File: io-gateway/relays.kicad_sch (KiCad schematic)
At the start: 24 parts, among them K1 2071556-2, K2 2071556-2, K3 2071556-2, K4 2071556-2, K5 2071556-2, K6 2071556-2, Q1 NTR4003NT1G, Q2 NTR4003NT1G, Q3 NTR4003NT1G, Q4 NTR4003NT1G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

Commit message: layout for first dimmer
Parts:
- K1, K2, K3, K4, K5, K6: footprint 20715562 -> Relay:20715562
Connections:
- net VAC_IN_1: no longer K2.4 (NO)
- net VAC_IN_2: now also K2.4 (NO); no longer K3.4 (NO), K4.4 (NO)
- net VAC_IN_3: now also K3.4 (NO); no longer K5.4 (NO), K6.4 (NO)
- net VAC_OUT_1.1 renamed VAC_OUT_1
- net VAC_OUT_1.2 renamed VAC_OUT_2
- net VAC_OUT_2.1 renamed VAC_OUT_3
- net VAC_OUT_2.2 renamed VAC_OUT_4
- net VAC_OUT_3.1 renamed VAC_OUT_5
- net VAC_OUT_3.2 renamed VAC_OUT_6
- new net VAC_IN_4: K4.4 (NO)
- new net VAC_IN_5: K5.4 (NO)
- new net VAC_IN_6: K6.4 (NO)
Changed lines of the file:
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@@
 	(wire
 		(pts
+			(xy 129.54 38.1) (xy 129.54 45.72)
+		)
+		(stroke
+			(width 0)
+			(type default)
+		)
+	)
+	(wire
+		(pts
 			(xy 190.5 40.64) (xy 190.5 46.99)
 		)
@@
 	(wire
 		(pts
-			(xy 35.56 58.42) (xy 35.56 71.12)
+			(xy 200.66 72.39) (xy 200.66 67.31)
 		)
 		(stroke
@@
 	(wire
 		(pts
-			(xy 119.38 152.4) (xy 119.38 157.48)
+			(xy 35.56 58.42) (xy 35.56 71.12)
 		)
 		(stroke
@@
 	(wire
 		(pts
-			(xy 204.47 38.1) (xy 200.66 38.1)
+			(xy 119.38 152.4) (xy 119.38 157.48)
 		)
 		(stroke
@@
 	(wire
 		(pts
+			(xy 129.54 72.39) (xy 137.16 72.39)
+		)
+		(stroke
+			(width 0)
+			(type default)
+		)
+	)
+	(wire
+		(pts
 			(xy 102.87 58.42) (xy 102.87 71.12)
 		)
@@
 	(wire
 		(pts
-			(xy 200.66 67.31) (xy 200.66 80.01)
-		)
-		(stroke
-			(width 0)
-			(type default)
-		)
-	)
-	(wire
-		(pts
 			(xy 190.5 67.31) (xy 190.5 72.39)
 		)
@@
 	(wire
 		(pts
-			(xy 129.54 72.39) (xy 138.43 72.39)
+			(xy 213.36 102.87) (xy 196.85 102.87)
 		)
 		(stroke
@@
 	(wire
 		(pts
-			(xy 213.36 102.87) (xy 196.85 102.87)
+			(xy 190.5 91.44) (xy 190.5 95.25)
 		)
 		(stroke
@@
 	(wire
 		(pts
-			(xy 190.5 91.44) (xy 190.5 95.25)
+			(xy 63.5 151.13) (xy 62.23 151.13)
 		)
 		(stroke
@@
 	(wire
 		(pts
-			(xy 63.5 151.13) (xy 62.23 151.13)
+			(xy 173.99 83.82) (xy 180.34 83.82)
 		)
 		(stroke
@@
 	(wire
 		(pts
-			(xy 173.99 83.82) (xy 180.34 83.82)
+			(xy 62.23 44.45) (xy 62.23 38.1)
 		)
 		(stroke
@@
 	(wire
 		(pts
-			(xy 62.23 44.45) (xy 62.23 38.1)
+			(xy 213.36 129.54) (xy 213.36 134.62)
 		)
 		(stroke
@@
 	(wire
 		(pts
-			(xy 213.36 129.54) (xy 213.36 134.62)
+			(xy 196.85 102.87) (xy 196.85 114.3)
 		)
 		(stroke
@@
 	(wire
 		(pts
-			(xy 196.85 102.87) (xy 196.85 114.3)
+			(xy 200.66 38.1) (xy 204.47 38.1)
 		)
 		(stroke
@@
 	(wire
 		(pts
-			(xy 190.5 40.64) (xy 173.99 40.64)
+			(xy 204.47 72.39) (xy 200.66 72.39)
 		)
 		(stroke
@@
 	(wire
 		(pts
-			(xy 129.54 40.64) (xy 129.54 45.72)
+			(xy 190.5 40.64) (xy 173.99 40.64)
 		)
 		(stroke
@@
 	(wire
 		(pts
+			(xy 134.62 38.1) (xy 129.54 38.1)
+		)
+		(stroke
+			(width 0)
+			(type default)
+		)
+	)
+	(wire
+		(pts
 			(xy 35.56 163.83) (xy 41.91 163.83)
 		)
@@
 		)
 	)
-	(global_label "VAC_IN_3"
+	(global_label "VAC_IN_5"
 		(shape input)
 		(at 132.08 156.21 0)
@@
 		)
 	)
-	(global_label "VAC_OUT_1.2"
+	(global_label "VAC_IN_3"
 		(shape input)
-		(at 129.54 40.64 0)
+		(at 204.47 72.39 0)
 		(fields_autoplaced yes)
 		(effects
@@
 		)
 		(property "Intersheetrefs" "${INTERSHEET_REFS}"
-			(at 144.56 40.64 0)
+			(at 215.9824 72.39 0)
 			(effects
 				(font
@@
 		)
 	)
-	(global_label "VAC_IN_1"
+	(global_label "VAC_IN_4"
 		(shape input)
-		(at 138.43 72.39 0)
+		(at 63.5 151.13 0)
 		(fields_autoplaced yes)
 		(effects
@@
 		)
 		(property "Intersheetrefs" "${INTERSHEET_REFS}"
-			(at 149.9424 72.39 0)
+			(at 75.0124 151.13 0)
 			(effects
 				(font
@@
 	(global_label "VAC_IN_2"
 		(shape input)
-		(at 200.66 80.01 0)
+		(at 137.16 72.39 0)
 		(fields_autoplaced yes)
 		(effects
@@
 		)
 		(property "Intersheetrefs" "${INTERSHEET_REFS}"
-			(at 212.1724 80.01 0)
+			(at 148.6724 72.39 0)
 			(effects
 				(font
@@
 		)
 	)
-	(global_label "VAC_IN_2"
+	(global_label "VAC_IN_6"
 		(shape input)
-		(at 63.5 151.13 0)
+		(at 226.06 134.62 0)
 		(fields_autoplaced yes)
 		(effects
@@
 		)
 		(property "Intersheetrefs" "${INTERSHEET_REFS}"
-			(at 75.0124 151.13 0)
+			(at 237.5724 134.62 0)
 			(effects
 				(font
@@
 		)
 	)
-	(global_label "VAC_IN_3"
+	(global_label "VAC_OUT_5"
 		(shape input)
-		(at 226.06 134.62 0)
+		(at 132.08 125.73 0)
 		(fields_autoplaced yes)
 		(effects
@@
 		)
 		(property "Intersheetrefs" "${INTERSHEET_REFS}"
-			(at 237.5724 134.62 0)
+			(at 145.2857 125.73 0)
 			(effects
 				(font
@@
 		)
 	)
-	(global_label "VAC_OUT_3.1"
+	(global_label "VAC_OUT_6"
 		(shape input)
-		(at 132.08 125.73 0)
+		(at 226.06 102.87 0)
 		(fields_autoplaced yes)
 		(effects
@@
 		)
 		(property "Intersheetrefs" "${INTERSHEET_REFS}"
-			(at 147.1 125.73 0)
+			(at 239.2657 102.87 0)
 			(effects
 				(font
@@
 		)
 	)
-	(global_label "VAC_OUT_3.2"
+	(global_label "VAC_OUT_1"
 		(shape input)
-		(at 226.06 102.87 0)
+		(at 64.77 38.1 0)
 		(fields_autoplaced yes)
 		(effects
@@
 		)
 		(property "Intersheetrefs" "${INTERSHEET_REFS}"
-			(at 241.08 102.87 0)
+			(at 77.9757 38.1 0)
 			(effects
 				(font
@@
 		)
 	)
-	(global_label "VAC_OUT_1.1"
+	(global_label "VAC_OUT_4"
 		(shape input)
-		(at 64.77 38.1 0)
+		(at 64.77 120.65 0)
 		(fields_autoplaced yes)
 		(effects
@@
 		)
 		(property "Intersheetrefs" "${INTERSHEET_REFS}"
-			(at 79.79 38.1 0)
+			(at 77.9757 120.65 0)
 			(effects
 				(font
@@
 		)
 	)
-	(global_label "VAC_OUT_2.2"
+	(global_label "VAC_OUT_2"
 		(shape input)
-		(at 64.77 120.65 0)
+		(at 134.62 38.1 0)
 		(fields_autoplaced yes)
 		(effects
@@
 		)
 		(property "Intersheetrefs" "${INTERSHEET_REFS}"
-			(at 79.79 120.65 0)
+			(at 147.8257 38.1 0)
 			(effects
 				(font
@@
 		)
 	)
-	(global_label "VAC_OUT_2.1"
+	(global_label "VAC_OUT_3"
 		(shape input)
 		(at 204.47 38.1 0)
@@
 		)
 		(property "Intersheetrefs" "${INTERSHEET_REFS}"
-			(at 219.49 38.1 0)
+			(at 217.6757 38.1 0)
 			(effects
 				(font
@@
 	)
 	(symbol
+		(lib_name "2071556-2_3")
 		(lib_id "2071556-2:2071556-2")
 		(at 195.58 50.8 0)
@@
 			)
 		)
-		(property "Footprint" "20715562"
+		(property "Footprint" "Relay:20715562"
 			(at 222.25 145.72 0)
 			(effects
@@
 		(pin "2"
 		)
-		(pin "14"
-		)
-		(pin "8"
-		)
 		(instances
 			(project "io-gateway"
@@
 	)
 	(symbol
+		(lib_name "2071556-2_1")
 		(lib_id "2071556-2:2071556-2")
 		(at 57.15 48.26 0)
@@
 			)
 		)
-		(property "Footprint" "20715562"
+		(property "Footprint" "Relay:20715562"
 			(at 83.82 143.18 0)
 			(effects
@@
 		(pin "2"
 		)
-		(pin "8"
-		)
-		(pin "14"
-		)
 		(instances
 			(project "io-gateway"
@@
 			)
 		)
-		(property "Footprint" "20715562"
+		(property "Footprint" "Relay:20715562"
 			(at 245.11 207.95 0)
 			(effects
@@
 		(pin "2"
 		)
-		(pin "14"
-		)
-		(pin "8"
-		)
 		(instances
 			(project "io-gateway"
@@
 	)
 	(symbol
+		(lib_name "2071556-2_4")
 		(lib_id "2071556-2:2071556-2")
 		(at 57.15 130.81 0)
@@
 			)
 		)
-		(property "Footprint" "20715562"
+		(property "Footprint" "Relay:20715562"
 			(at 83.82 225.73 0)
 			(effects
@@
 		(pin "2"
 		)
-		(pin "8"
-		)
-		(pin "14"
-		)
 		(instances
 			(project "io-gateway"
@@
 	)
 	(symbol
+		(lib_name "2071556-2_2")
 		(lib_id "2071556-2:2071556-2")
 		(at 124.46 49.53 0)
@@
 			)
 		)
-		(property "Footprint" "20715562"
+		(property "Footprint" "Relay:20715562"
 			(at 151.13 144.45 0)
 			(effects
@@
 		(pin "2"
 		)
-		(pin "8"
-		)
-		(pin "14"
-		)
 		(instances
 			(project "io-gateway"
@@
 	)
 	(symbol
+		(lib_name "2071556-2_5")
 		(lib_id "2071556-2:2071556-2")
 		(at 124.46 135.89 0)
@@
 			)
 		)
-		(property "Footprint" "20715562"
+		(property "Footprint" "Relay:20715562"
 			(at 151.13 230.81 0)
 			(effects
@@
 		(pin "2"
 		)
-		(pin "8"
-		)
-		(pin "14"
-		)
 		(instances

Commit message: temp
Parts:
- removed D3, D4, D5, D6, D7: MMSD914, Diode_SMD:D_SOD-123, symbol Diode:MMSD914
- removed K2, K3, K4, K5, K6: 2071556-2, Relay:20715562, symbol 2071556-2:2071556-2
- removed Q2, Q3, Q4, Q5, Q6: NTR4003NT1G, Package_TO_SOT_SMD:SOT-23-3, symbol NTR4003NT1G:NTR4003NT1G
- removed R13, R22, R23, R24, R25: 100, Resistor_SMD:R_0603_1608Metric, symbol Device:R
- renumbered D2 to D_K, Q1 to Q_K, R10 to R_K
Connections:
- net SW_IN: now reaches R_K.1
- net VAC_IN_1 renamed VAC_IN
- net VAC_OUT_1 renamed VAC_OUT
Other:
- moved on the sheet: D_K, K1, Q_K, R_K

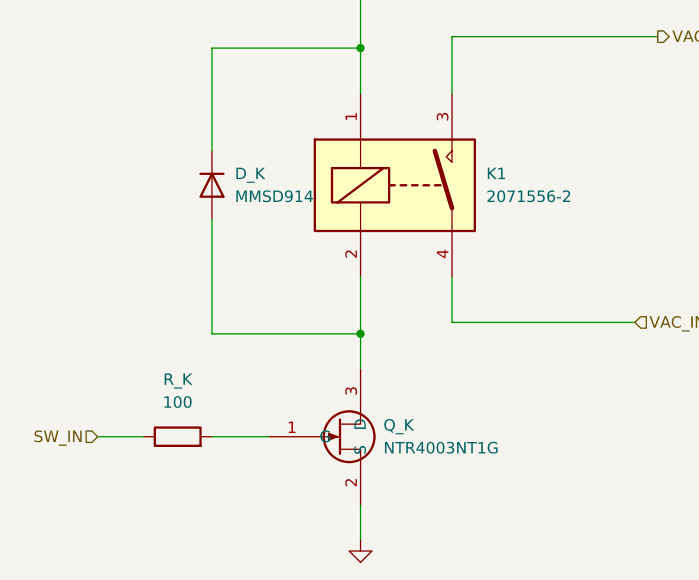
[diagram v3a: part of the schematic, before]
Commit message: reannotate dimmers and relays
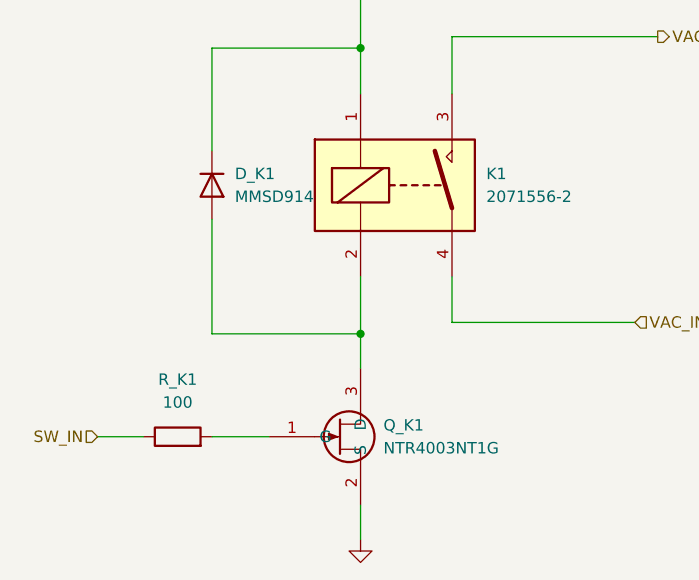
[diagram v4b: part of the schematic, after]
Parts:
- renumbered D_K to D_K1, Q_K to Q_K1, R_K to R_K1
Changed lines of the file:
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@@
 		(dnp no)
 		(fields_autoplaced yes)
-		(property "Reference" "#PWR"
+		(property "Reference" "#PWR015"
 			(at 99.06 48.26 0)
 			(effects
@@
 				)
 				(path "/2cb6f94b-272a-4ed7-b08d-c3630bda6156/8976081a-0d1c-4632-aadf-dea88614b0a1"
-					(reference "#PWR015")
+					(reference "#PWR0102")
 					(unit 1)
 				)
 				(path "/2cb6f94b-272a-4ed7-b08d-c3630bda6156/9d77d6d3-b511-418e-8a79-d9ff43bc2b57"
 					(reference "#PWR011")
+					(unit 1)
+				)
+				(path "/2cb6f94b-272a-4ed7-b08d-c3630bda6156/b7c52a2f-c911-47bd-b8aa-349b31ff8e17"
+					(reference "#PWR015")
 					(unit 1)
 				)
@@
 		(dnp no)
 		(fields_autoplaced yes)
-		(property "Reference" "R_K"
+		(property "Reference" "R_K1"
 			(at 78.74 88.9 90)
 			(effects
@@
 				(path "/2cb6f94b-272a-4ed7-b08d-c3630bda6156/9d77d6d3-b511-418e-8a79-d9ff43bc2b57"
 					(reference "R_K7")
+					(unit 1)
+				)
+				(path "/2cb6f94b-272a-4ed7-b08d-c3630bda6156/b7c52a2f-c911-47bd-b8aa-349b31ff8e17"
+					(reference "R_K1")
 					(unit 1)
 				)
@@
 		(dnp no)
 		(fields_autoplaced yes)
-		(property "Reference" "D_K"
+		(property "Reference" "D_K1"
 			(at 85.09 66.0399 90)
 			(effects
@@
 				(path "/2cb6f94b-272a-4ed7-b08d-c3630bda6156/9d77d6d3-b511-418e-8a79-d9ff43bc2b57"
 					(reference "D_K7")
+					(unit 1)
+				)
+				(path "/2cb6f94b-272a-4ed7-b08d-c3630bda6156/b7c52a2f-c911-47bd-b8aa-349b31ff8e17"
+					(reference "D_K1")
 					(unit 1)
 				)
@@
 		(dnp no)
 		(fields_autoplaced yes)
-		(property "Reference" "Q_K"
+		(property "Reference" "Q_K1"
 			(at 101.6 93.9799 0)
 			(effects
@@
 				(path "/2cb6f94b-272a-4ed7-b08d-c3630bda6156/9d77d6d3-b511-418e-8a79-d9ff43bc2b57"
 					(reference "Q_K7")
+					(unit 1)
+				)
+				(path "/2cb6f94b-272a-4ed7-b08d-c3630bda6156/b7c52a2f-c911-47bd-b8aa-349b31ff8e17"
+					(reference "Q_K1")
 					(unit 1)
 				)
@@
 		(dnp no)
 		(fields_autoplaced yes)
-		(property "Reference" "#PWR"
+		(property "Reference" "#PWR016"
 			(at 99.06 113.03 0)
 			(effects
@@
 				)
 				(path "/2cb6f94b-272a-4ed7-b08d-c3630bda6156/8976081a-0d1c-4632-aadf-dea88614b0a1"
-					(reference "#PWR016")
+					(reference "#PWR0101")
 					(unit 1)
 				)
@@
 					(unit 1)
 				)
+				(path "/2cb6f94b-272a-4ed7-b08d-c3630bda6156/b7c52a2f-c911-47bd-b8aa-349b31ff8e17"
+					(reference "#PWR016")
+					(unit 1)
+				)

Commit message: order V1.0
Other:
- moved on the sheet: D_K1
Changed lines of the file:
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@@
 	(wire
 		(pts
-			(xy 82.55 71.12) (xy 82.55 83.82)
-		)
-		(stroke
-			(width 0)
-			(type default)
-		)
-	)
-	(wire
-		(pts
-			(xy 82.55 52.07) (xy 82.55 63.5)
-		)
-		(stroke
-			(width 0)
-			(type default)
-		)
-	)
-	(wire
-		(pts
-			(xy 99.06 52.07) (xy 82.55 52.07)
+			(xy 77.47 71.12) (xy 77.47 83.82)
+		)
+		(stroke
+			(width 0)
+			(type default)
+		)
+	)
+	(wire
+		(pts
+			(xy 77.47 52.07) (xy 77.47 63.5)
+		)
+		(stroke
+			(width 0)
+			(type default)
+		)
+	)
+	(wire
+		(pts
+			(xy 99.06 52.07) (xy 77.47 52.07)
 		)
 		(stroke
@@
 	(wire
 		(pts
-			(xy 82.55 83.82) (xy 99.06 83.82)
+			(xy 77.47 83.82) (xy 99.06 83.82)
 		)
 		(stroke
@@
 	(symbol
 		(lib_id "Diode:MMSD914")
-		(at 82.55 67.31 270)
+		(at 77.47 67.31 270)
 		(unit 1)
 		(exclude_from_sim no)
@@
 		(fields_autoplaced yes)
 		(property "Reference" "D_K1"
-			(at 85.09 66.0399 90)
+			(at 80.01 66.0399 90)
 			(effects
 				(font
@@
 		)
 		(property "Value" "MMSD914"
-			(at 85.09 68.5799 90)
+			(at 80.01 68.5799 90)
 			(effects
 				(font
@@
 		)
 		(property "Footprint" "Diode_SMD:D_SOD-123"
-			(at 78.105 67.31 0)
+			(at 73.025 67.31 0)
 			(effects
 				(font
@@
 		)
 		(property "Datasheet" "https://www.onsemi.com/pub/Collateral/MMSD914T1-D.PDF"
-			(at 82.55 67.31 0)
+			(at 77.47 67.31 0)
 			(effects
 				(font
@@
 		)
 		(property "Description" "100V 0.2A Switching Diode, SOD-123"
-			(at 82.55 67.31 0)
+			(at 77.47 67.31 0)
 			(effects
 				(font
@@
 		)
 		(property "Sim.Device" "D"
-			(at 82.55 67.31 0)
+			(at 77.47 67.31 0)
 			(effects
 				(font
@@
 		)
 		(property "Sim.Pins" "1=K 2=A"
-			(at 82.55 67.31 0)
-			(effects
-				(font
+			(at 77.47 67.31 0)
+			(effects
+				(font
